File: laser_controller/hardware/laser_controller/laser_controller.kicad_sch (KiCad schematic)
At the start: 129 parts, among them J1 AudioJack2_SwitchT, J2 AudioJack2_SwitchT, J3 AudioJack2_SwitchT, J4 AudioJack2_SwitchT, J5 AudioJack2_SwitchT, J6 Conn_02x05_Odd_Even, J7 USB_C_Receptacle_USB2.0, J9 SI-46001-F, SW2 SW_Push, SW3 SW_Push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

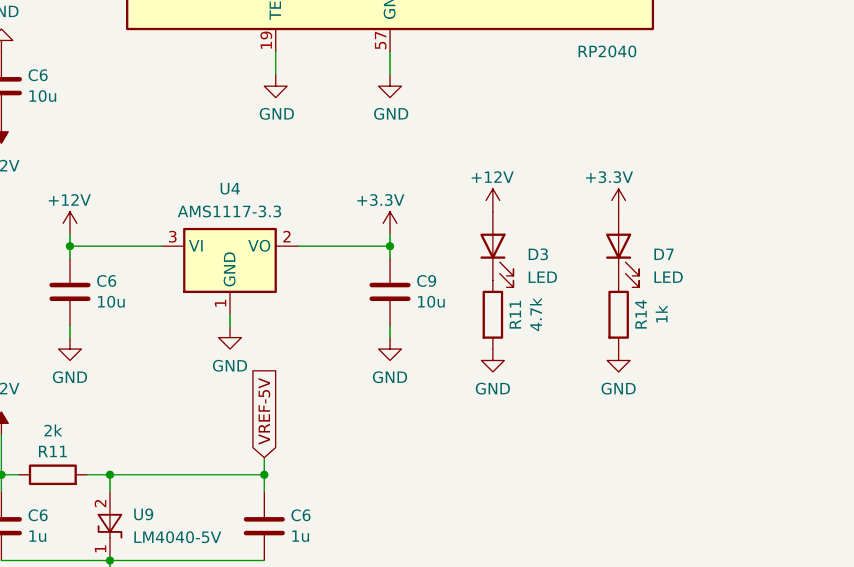
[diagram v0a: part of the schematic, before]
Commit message: Replaced 3.3V regulator
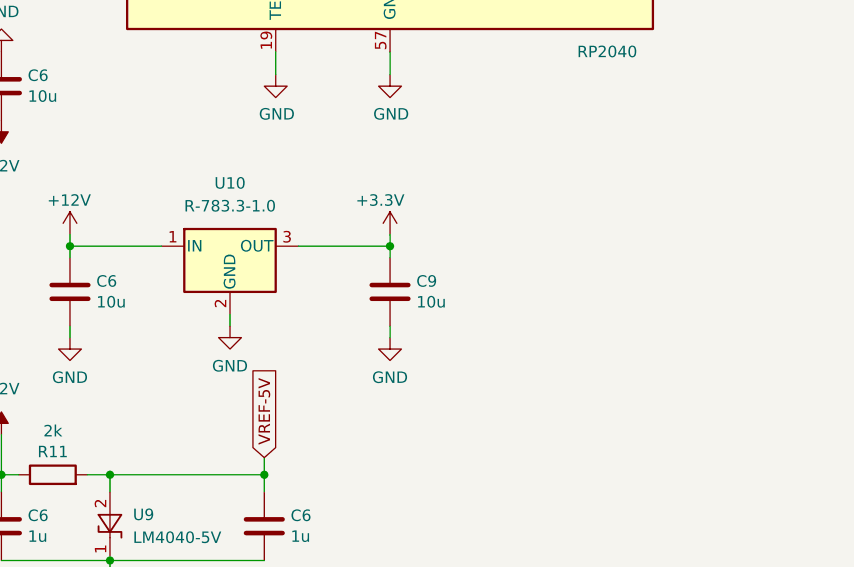
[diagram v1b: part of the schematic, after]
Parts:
- removed D3, D7: LED, LED_SMD:LED_0603_1608Metric, symbol Device:LED
- removed R11: 4.7k, Resistor_SMD:R_0603_1608Metric, symbol Device:R
- removed R14: 1k, Resistor_SMD:R_0603_1608Metric, symbol Device:R
- removed U4: AMS1117-3.3, Package_TO_SOT_SMD:SOT-223-3_TabPin2, symbol Regulator_Linear:AMS1117-3.3
- added U10: R-783.3-1.0, Converter_DCDC:Converter_DCDC_RECOM_R-78E-0.5_THT, symbol Regulator_Switching:R-783.3-1.0
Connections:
- net +12V: now also U10.1 (IN)
- net +3.3V: now also U10.3 (OUT)
- net GND: now also U10.2 (GND)

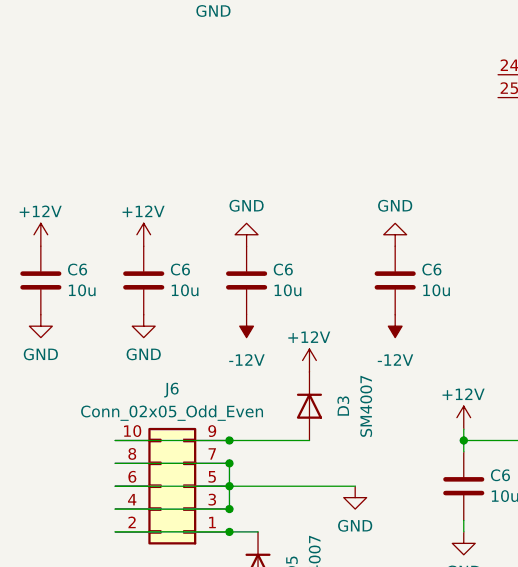
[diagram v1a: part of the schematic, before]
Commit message: Added electrolytic caps
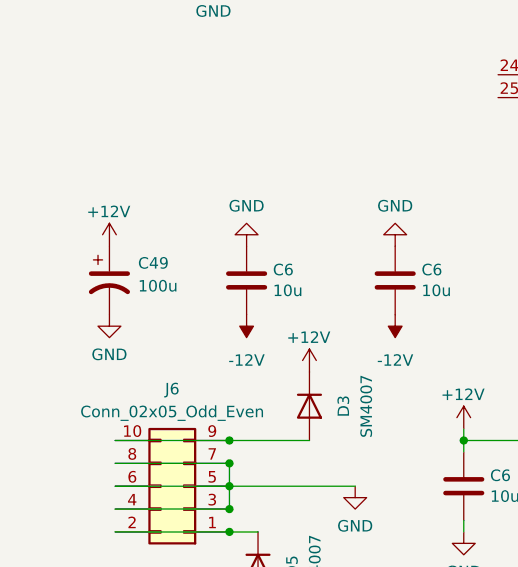
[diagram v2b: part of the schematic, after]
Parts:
- removed C6 (x2): 10u, Capacitor_SMD:C_0603_1608Metric, symbol Device:C
- added C49: 100u, Capacitor_SMD:CP_Elec_6.3x5.4, symbol Device:C_Polarized_US
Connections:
- net +12V: now also C49.1
- net GND: now also C49.2
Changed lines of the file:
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@@
     )
   )
-  (symbol (lib_id "PCM_4ms_Power-symbol:+12V") (at 31.115 163.195 0) (unit 1)
-    (in_bom yes) (on_board yes) (dnp no)
-    (property "Reference" "#PWR049" (at 31.115 167.005 0)
-      (effects (font (size 1.27 1.27)) hide)
-    )
-    (property "Value" "+12V" (at 28.575 159.385 0)
-      (effects (font (size 1.27 1.27)) (justify left))
-    )
-    (property "Footprint" "" (at 31.115 163.195 0)
-      (effects (font (size 1.27 1.27)) hide)
-    )
-    (property "Datasheet" "" (at 31.115 163.195 0)
-      (effects (font (size 1.27 1.27)) hide)
-    )
-    (pin "1")
-    (instances
-      (project "jukebox_light_controller"
-        (path "/3d7cdb1e-a810-4ff2-a852-82c48438ee64"
-          (reference "#PWR049") (unit 1)
-        )
-      )
-      (project "laser_controller"
-        (path "/66f4951c-8ca6-44d4-8426-28e02ddf3b18"
-          (reference "#PWR035") (unit 1)
-        )
-      )
-      (project "canbus_adapter"
-        (path "/805386a4-6883-4c41-8ba1-2a13d67886f6"
-          (reference "#PWR094") (unit 1)
-        )
-      )
-      (project "combo_laser_driver"
-        (path "/e63e39d7-6ac0-4ffd-8aa3-1841a4541b55"
-          (reference "#PWR032") (unit 1)
-        )
-      )
-    )
-  )
   (symbol (lib_id "Device:R") (at 361.315 49.53 180) (unit 1)
     (in_bom yes) (on_board yes) (dnp no)
@@
     )
   )
+  (symbol (lib_id "Device:C_Polarized_US") (at 27.305 167.005 0) (unit 1)
+    (in_bom yes) (on_board yes) (dnp no) (fields_autoplaced)
+    (property "Reference" "C49" (at 30.48 165.1 0)
+      (effects (font (size 1.27 1.27)) (justify left))
+    )
+    (property "Value" "100u" (at 30.48 167.64 0)
+      (effects (font (size 1.27 1.27)) (justify left))
+    )
+    (property "Footprint" "Capacitor_SMD:CP_Elec_6.3x5.4" (at 27.305 167.005 0)
+      (effects (font (size 1.27 1.27)) hide)
+    )
+    (property "Datasheet" "~" (at 27.305 167.005 0)
+      (effects (font (size 1.27 1.27)) hide)
+    )
+    (pin "1")
+    (pin "2")
+    (instances
+      (project "laser_controller"
+        (path "/66f4951c-8ca6-44d4-8426-28e02ddf3b18"
+          (reference "C49") (unit 1)
+        )
+      )
+    )
+  )
   (symbol (lib_id "power:GND") (at 84.455 193.675 0) (unit 1)
     (in_bom yes) (on_board yes) (dnp no)
@@
     )
   )
-  (symbol (lib_id "Device:C") (at 31.115 167.005 0) (unit 1)
-    (in_bom yes) (on_board yes) (dnp no)
-    (property "Reference" "C6" (at 34.036 165.8366 0)
-      (effects (font (size 1.27 1.27)) (justify left))
-    )
-    (property "Value" "10u" (at 34.036 168.148 0)
-      (effects (font (size 1.27 1.27)) (justify left))
-    )
-    (property "Footprint" "Capacitor_SMD:C_0603_1608Metric" (at 32.0802 170.815 0)
-      (effects (font (size 1.27 1.27)) hide)
-    )
-    (property "Datasheet" "~" (at 31.115 167.005 0)
-      (effects (font (size 1.27 1.27)) hide)
-    )
-    (pin "1")
-    (pin "2")
-    (instances
-      (project "jukebox_light_controller"
-        (path "/3d7cdb1e-a810-4ff2-a852-82c48438ee64"
-          (reference "C6") (unit 1)
-        )
-      )
-      (project "laser_controller"
-        (path "/66f4951c-8ca6-44d4-8426-28e02ddf3b18"
-          (reference "C46") (unit 1)
-        )
-      )
-      (project "canbus_adapter"
-        (path "/805386a4-6883-4c41-8ba1-2a13d67886f6"
-          (reference "C3") (unit 1)
-        )
-      )
-      (project "RP2040_minimal"
-        (path "/82a49de2-ec1b-43dd-97fe-0b636089eb84"
-          (reference "C1") (unit 1)
-        )
-      )
-      (project "combo_laser_driver"
-        (path "/e63e39d7-6ac0-4ffd-8aa3-1841a4541b55"
-          (reference "C2") (unit 1)
-        )
-      )
-    )
-  )
   (symbol (lib_id "Device:R") (at 299.085 179.705 0) (unit 1)
     (in_bom yes) (on_board yes) (dnp no)
@@
     )
   )
-  (symbol (lib_id "power:GND") (at 19.685 170.815 0) (unit 1)
+  (symbol (lib_id "power:GND") (at 27.305 170.815 0) (unit 1)
     (in_bom yes) (on_board yes) (dnp no)
-    (property "Reference" "#PWR044" (at 19.685 177.165 0)
+    (property "Reference" "#PWR044" (at 27.305 177.165 0)
       (effects (font (size 1.27 1.27)) hide)
     )
-    (property "Value" "GND" (at 19.685 175.26 0)
+    (property "Value" "GND" (at 27.305 175.26 0)
       (effects (font (size 1.27 1.27)))
     )
-    (property "Footprint" "" (at 19.685 170.815 0)
+    (property "Footprint" "" (at 27.305 170.815 0)
       (effects (font (size 1.27 1.27)) hide)
     )
-    (property "Datasheet" "" (at 19.685 170.815 0)
+    (property "Datasheet" "" (at 27.305 170.815 0)
       (effects (font (size 1.27 1.27)) hide)
     )
@@
     )
   )
-  (symbol (lib_id "PCM_4ms_Power-symbol:+12V") (at 19.685 163.195 0) (unit 1)
+  (symbol (lib_id "PCM_4ms_Power-symbol:+12V") (at 27.305 163.195 0) (unit 1)
     (in_bom yes) (on_board yes) (dnp no)
-    (property "Reference" "#PWR049" (at 19.685 167.005 0)
+    (property "Reference" "#PWR049" (at 27.305 167.005 0)
       (effects (font (size 1.27 1.27)) hide)
     )
-    (property "Value" "+12V" (at 17.145 159.385 0)
+    (property "Value" "+12V" (at 24.765 159.385 0)
       (effects (font (size 1.27 1.27)) (justify left))
     )
-    (property "Footprint" "" (at 19.685 163.195 0)
+    (property "Footprint" "" (at 27.305 163.195 0)
       (effects (font (size 1.27 1.27)) hide)
     )
-    (property "Datasheet" "" (at 19.685 163.195 0)
+    (property "Datasheet" "" (at 27.305 163.195 0)
       (effects (font (size 1.27 1.27)) hide)
     )
@@
     )
   )
-  (symbol (lib_id "power:GND") (at 31.115 170.815 0) (unit 1)
-    (in_bom yes) (on_board yes) (dnp no)
-    (property "Reference" "#PWR044" (at 31.115 177.165 0)
-      (effects (font (size 1.27 1.27)) hide)
-    )
-    (property "Value" "GND" (at 31.115 175.26 0)
-      (effects (font (size 1.27 1.27)))
-    )
-    (property "Footprint" "" (at 31.115 170.815 0)
-      (effects (font (size 1.27 1.27)) hide)
-    )
-    (property "Datasheet" "" (at 31.115 170.815 0)
-      (effects (font (size 1.27 1.27)) hide)
-    )
-    (pin "1")
-    (instances
-      (project "jukebox_light_controller"
-        (path "/3d7cdb1e-a810-4ff2-a852-82c48438ee64"
-          (reference "#PWR044") (unit 1)
-        )
-      )
-      (project "laser_controller"
-        (path "/66f4951c-8ca6-44d4-8426-28e02ddf3b18"
-          (reference "#PWR036") (unit 1)
-        )
-      )
-      (project "canbus_adapter"
-        (path "/805386a4-6883-4c41-8ba1-2a13d67886f6"
-          (reference "#PWR014") (unit 1)
-        )
-      )
-      (project "RP2040_minimal"
-        (path "/82a49de2-ec1b-43dd-97fe-0b636089eb84"
-          (reference "#PWR05") (unit 1)
-        )
-      )
-      (project "combo_laser_driver"
-        (path "/e63e39d7-6ac0-4ffd-8aa3-1841a4541b55"
-          (reference "#PWR029") (unit 1)
-        )
-      )
-    )
-  )
   (symbol (lib_id "Device:R_US") (at 281.305 94.615 270) (mirror x) (unit 1)
     (in_bom yes) (on_board yes) (dnp no)
@@
         )
       )
-    )
-  )
-  (symbol (lib_id "Device:C") (at 19.685 167.005 0) (unit 1)
-    (in_bom yes) (on_board yes) (dnp no)
-    (property "Reference" "C6" (at 22.606 165.8366 0)
-      (effects (font (size 1.27 1.27)) (justify left))
-    )
-    (property "Value" "10u" (at 22.606 168.148 0)
-      (effects (font (size 1.27 1.27)) (justify left))
-    )
-    (property "Footprint" "Capacitor_SMD:C_0603_1608Metric" (at 20.6502 170.815 0)
-      (effects (font (size 1.27 1.27)) hide)
-    )
-    (property "Datasheet" "~" (at 19.685 167.005 0)
-      (effects (font (size 1.27 1.27)) hide)
-    )
-    (pin "1")
-    (pin "2")
-    (instances
-      (project "jukebox_light_controller"
-        (path "/3d7cdb1e-a810-4ff2-a852-82c48438ee64"
-          (reference "C6") (unit 1)
-        )
-      )
-      (project "laser_controller"
-        (path "/66f4951c-8ca6-44d4-8426-28e02ddf3b18"
-          (reference "C43") (unit 1)
-        )
-      )
-      (project "canbus_adapter"
-        (path "/805386a4-6883-4c41-8ba1-2a13d67886f6"
-          (reference "C3") (unit 1)
-        )
-      )
-      (project "RP2040_minimal"
-        (path "/82a49de2-ec1b-43dd-97fe-0b636089eb84"
-          (reference "C1") (unit 1)
-        )
-      )
-      (project "combo_laser_driver"
-        (path "/e63e39d7-6ac0-4ffd-8aa3-1841a4541b55"
-          (reference "C2") (unit 1)
-        )
-      )
